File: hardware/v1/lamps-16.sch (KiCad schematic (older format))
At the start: 1 part, among them P7 CONN_02X05

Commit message: Manually route lmaps-16 board
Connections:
- net DIGITA: now also P7.4 (P4); no longer P7.9 (P9)
- net DIGITB: now also P7.6 (P6); no longer P7.10 (P10)
- net SEG0: now also P7.2 (P2); no longer P7.1 (P1)
- net SEG1: now also P7.1 (P1); no longer P7.2 (P2)
- net SEG3: now also P7.5 (P5); no longer P7.4 (P4)
- net SEG4: now also P7.7 (P7); no longer P7.5 (P5)
- net SEG5: now also P7.9 (P9); no longer P7.6 (P6)
- net SEG6: now also P7.10 (P10); no longer P7.7 (P7)
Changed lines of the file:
@@
 LIBS:contrib
 LIBS:valves
+LIBS:lamps-16-cache
 EELAYER 25 0
 EELAYER END
@@
 encoding utf-8
 Sheet 1 3
-Title ""
-Date ""
-Rev ""
-Comp ""
-Comment1 ""
+Title "LAMPS-16"
+Date "2016-08-05"
+Rev "1.0.0"
+Comp "University of Glasgow"
+Comment1 "Kristian Hentschel"
 Comment2 ""
 Comment3 ""
-Comment4 ""
+Comment4 "REDEUCE Control Panel"
 $EndDescr
 $Sheet
@@
 Text Label 3100 3200 2    60   ~ 0
 SEG7
+Text Label 1450 800  0    60   ~ 0
+SEG0
 Text Label 950  800  2    60   ~ 0
-SEG0
-Text Label 1450 800  0    60   ~ 0
 SEG1
 Text Label 950  900  2    60   ~ 0
 SEG2
+Text Label 950  1000 2    60   ~ 0
+SEG3
+Text Label 950  1100 2    60   ~ 0
+SEG4
+Text Label 950  1200 2    60   ~ 0
+SEG5
+Text Label 1450 1200 0    60   ~ 0
+SEG6
+Text Label 1450 1100 0    60   ~ 0
+SEG7
+Text Label 1000 2100 2    60   ~ 0
+SEG0
+Text Label 1000 2200 2    60   ~ 0
+SEG1
+Text Label 1000 2300 2    60   ~ 0
+SEG2
+Text Label 1000 2400 2    60   ~ 0
+SEG3
+Text Label 1000 2500 2    60   ~ 0
+SEG4
+Text Label 1000 2600 2    60   ~ 0
+SEG5
+Text Label 1000 2700 2    60   ~ 0
+SEG6
+Text Label 1000 2800 2    60   ~ 0
+SEG7
+Text Label 3100 800  2    60   ~ 0
+DIGITA
+Text Label 3100 2250 2    60   ~ 0
+DIGITB
+Text Label 1000 3050 2    60   ~ 0
+DIGITA
+Text Label 1000 3200 2    60   ~ 0
+DIGITB
+Text HLabel 1150 2050 2    60   Input ~ 0
+SEG0
+Text HLabel 1150 2150 2    60   Input ~ 0
+SEG1
+Text HLabel 1150 2250 2    60   Input ~ 0
+SEG2
+Text HLabel 1150 2350 2    60   Input ~ 0
+SEG3
+Text HLabel 1150 2450 2    60   Input ~ 0
+SEG4
+Text HLabel 1150 2550 2    60   Input ~ 0
+SEG5
+Text HLabel 1150 2650 2    60   Input ~ 0
+SEG6
+Text HLabel 1150 2750 2    60   Input ~ 0
+SEG7
+Text HLabel 1150 3000 2    60   Input ~ 0
+DIGITA
+Text HLabel 1150 3150 2    60   Input ~ 0
+DIGITB
+Wire Wire Line
+	1000 2100 1100 2100
+Wire Wire Line
+	1100 2100 1100 2050
+Wire Wire Line
+	1100 2050 1150 2050
+Wire Wire Line
+	1150 2150 1100 2150
+Wire Wire Line
+	1100 2150 1100 2200
+Wire Wire Line
+	1100 2200 1000 2200
+Wire Wire Line
+	1000 2300 1100 2300
+Wire Wire Line
+	1100 2300 1100 2250
+Wire Wire Line
+	1100 2250 1150 2250
+Wire Wire Line
+	1150 2350 1100 2350
+Wire Wire Line
+	1100 2350 1100 2400
+Wire Wire Line
+	1100 2400 1000 2400
+Wire Wire Line
+	1000 2500 1100 2500
+Wire Wire Line
+	1100 2500 1100 2450
+Wire Wire Line
+	1100 2450 1150 2450
+Wire Wire Line
+	1150 2550 1100 2550
+Wire Wire Line
+	1100 2550 1100 2600
+Wire Wire Line
+	1100 2600 1000 2600
+Wire Wire Line
+	1000 2700 1100 2700
+Wire Wire Line
+	1100 2700 1100 2650
+Wire Wire Line
+	1100 2650 1150 2650
+Wire Wire Line
+	1150 2750 1100 2750
+Wire Wire Line
+	1100 2750 1100 2800
+Wire Wire Line
+	1100 2800 1000 2800
+Wire Wire Line
+	1000 3050 1100 3050
+Wire Wire Line
+	1100 3050 1100 3000
+Wire Wire Line
+	1100 3000 1150 3000
+Wire Wire Line
+	1150 3150 1100 3150
+Wire Wire Line
+	1100 3150 1100 3200
+Wire Wire Line
+	1100 3200 1000 3200
 Text Label 1450 900  0    60   ~ 0
-SEG3
-Text Label 950  1000 2    60   ~ 0
-SEG4
+DIGITA
 Text Label 1450 1000 0    60   ~ 0
-SEG5
-Text Label 950  1100 2    60   ~ 0
-SEG6
-Text Label 1450 1100 0    60   ~ 0
-SEG7
-Wire Wire Line
-	3100 800  1850 800
-Wire Wire Line
-	600  1200 950  1200
-Wire Wire Line
-	600  1200 600  600
-Wire Wire Line
-	600  600  1850 600
-Wire Wire Line
-	1850 600  1850 800
-Wire Wire Line
-	1450 1200 1850 1200
-Wire Wire Line
-	1850 1200 1850 2250
-Wire Wire Line
-	1850 2250 3100 2250
-Text Label 1000 2100 2    60   ~ 0
-SEG0
-Text Label 1000 2200 2    60   ~ 0
-SEG1
-Text Label 1000 2300 2    60   ~ 0
-SEG2
-Text Label 1000 2400 2    60   ~ 0
-SEG3
-Text Label 1000 2500 2    60   ~ 0
-SEG4
-Text Label 1000 2600 2    60   ~ 0
-SEG5
-Text Label 1000 2700 2    60   ~ 0
-SEG6
-Text Label 1000 2800 2    60   ~ 0
-SEG7
-Text Label 2800 800  2    60   ~ 0
-DIGITA
-Text Label 2800 2250 2    60   ~ 0
-DIGITB
-Text Label 1000 3050 2    60   ~ 0
-DIGITA
-Text Label 1000 3200 2    60   ~ 0
-DIGITB
-Text HLabel 1150 2050 2    60   Input ~ 0
-SEG0
-Text HLabel 1150 2150 2    60   Input ~ 0
-SEG1
-Text HLabel 1150 2250 2    60   Input ~ 0
-SEG2
-Text HLabel 1150 2350 2    60   Input ~ 0
-SEG3
-Text HLabel 1150 2450 2    60   Input ~ 0
-SEG4
-Text HLabel 1150 2550 2    60   Input ~ 0
-SEG5
-Text HLabel 1150 2650 2    60   Input ~ 0
-SEG6
-Text HLabel 1150 2750 2    60   Input ~ 0
-SEG7
-Text HLabel 1150 3000 2    60   Input ~ 0
-DIGITA
-Text HLabel 1150 3150 2    60   Input ~ 0
-DIGITB
-Wire Wire Line
-	1000 2100 1100 2100
-Wire Wire Line
-	1100 2100 1100 2050
-Wire Wire Line
-	1100 2050 1150 2050
-Wire Wire Line
-	1150 2150 1100 2150
-Wire Wire Line
-	1100 2150 1100 2200
-Wire Wire Line
-	1100 2200 1000 2200
-Wire Wire Line
-	1000 2300 1100 2300
-Wire Wire Line
-	1100 2300 1100 2250
-Wire Wire Line
-	1100 2250 1150 2250
-Wire Wire Line
-	1150 2350 1100 2350
-Wire Wire Line
-	1100 2350 1100 2400
-Wire Wire Line
-	1100 2400 1000 2400
-Wire Wire Line
-	1000 2500 1100 2500
-Wire Wire Line
-	1100 2500 1100 2450
-Wire Wire Line
-	1100 2450 1150 2450
-Wire Wire Line
-	1150 2550 1100 2550
-Wire Wire Line
-	1100 2550 1100 2600
-Wire Wire Line
-	1100 2600 1000 2600
-Wire Wire Line
-	1000 2700 1100 2700
-Wire Wire Line
-	1100 2700 1100 2650
-Wire Wire Line
-	1100 2650 1150 2650
-Wire Wire Line
-	1150 2750 1100 2750
-Wire Wire Line
-	1100 2750 1100 2800
-Wire Wire Line
-	1100 2800 1000 2800
-Wire Wire Line
-	1000 3050 1100 3050
-Wire Wire Line
-	1100 3050 1100 3000
-Wire Wire Line
-	1100 3000 1150 3000
-Wire Wire Line
-	1150 3150 1100 3150
-Wire Wire Line
-	1100 3150 1100 3200
-Wire Wire Line
-	1100 3200 1000 3200
+DIGITB
 $EndSCHEMATC

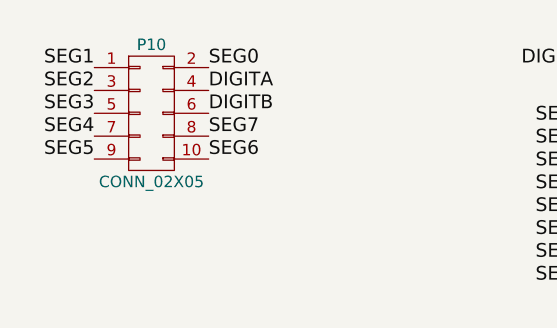
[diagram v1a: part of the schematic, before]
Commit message: Correct lamps-16 connector layout in piconnect board.
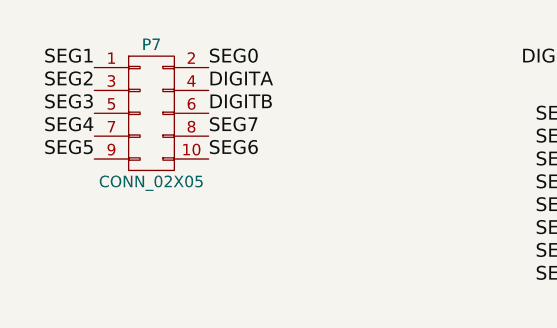
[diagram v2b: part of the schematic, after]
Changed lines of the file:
@@
 LIBS:contrib
 LIBS:valves
-LIBS:lamps-16-cache
+LIBS:MAX7221
+LIBS:MCP23S17
+LIBS:MCP23017
+LIBS:Pi2_Connector
+LIBS:v1-cache
 EELAYER 25 0
 EELAYER END
 $Descr A4 11693 8268
 encoding utf-8
-Sheet 1 3
+Sheet 11 22
 Title "LAMPS-16"
 Date "2016-08-05"
@@
 AR Path="/57A56122/57A3FFF5" Ref="P10"  Part="1"
 AR Path="/57A3FFF5" Ref="P10"  Part="1"
-F 0 "P10" H 1200 1300 50  0000 C CNN
+F 0 "P7" H 1200 1300 50  0000 C CNN
 F 1 "CONN_02X05" H 1200 700 50  0000 C CNN
 F 2 "Pin_Headers:Pin_Header_Angled_2x05" H 1200 -200 50  0001 C CNN
